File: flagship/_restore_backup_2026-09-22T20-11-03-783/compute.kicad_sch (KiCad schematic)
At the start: 1 part, among them U1 STAMP_P4

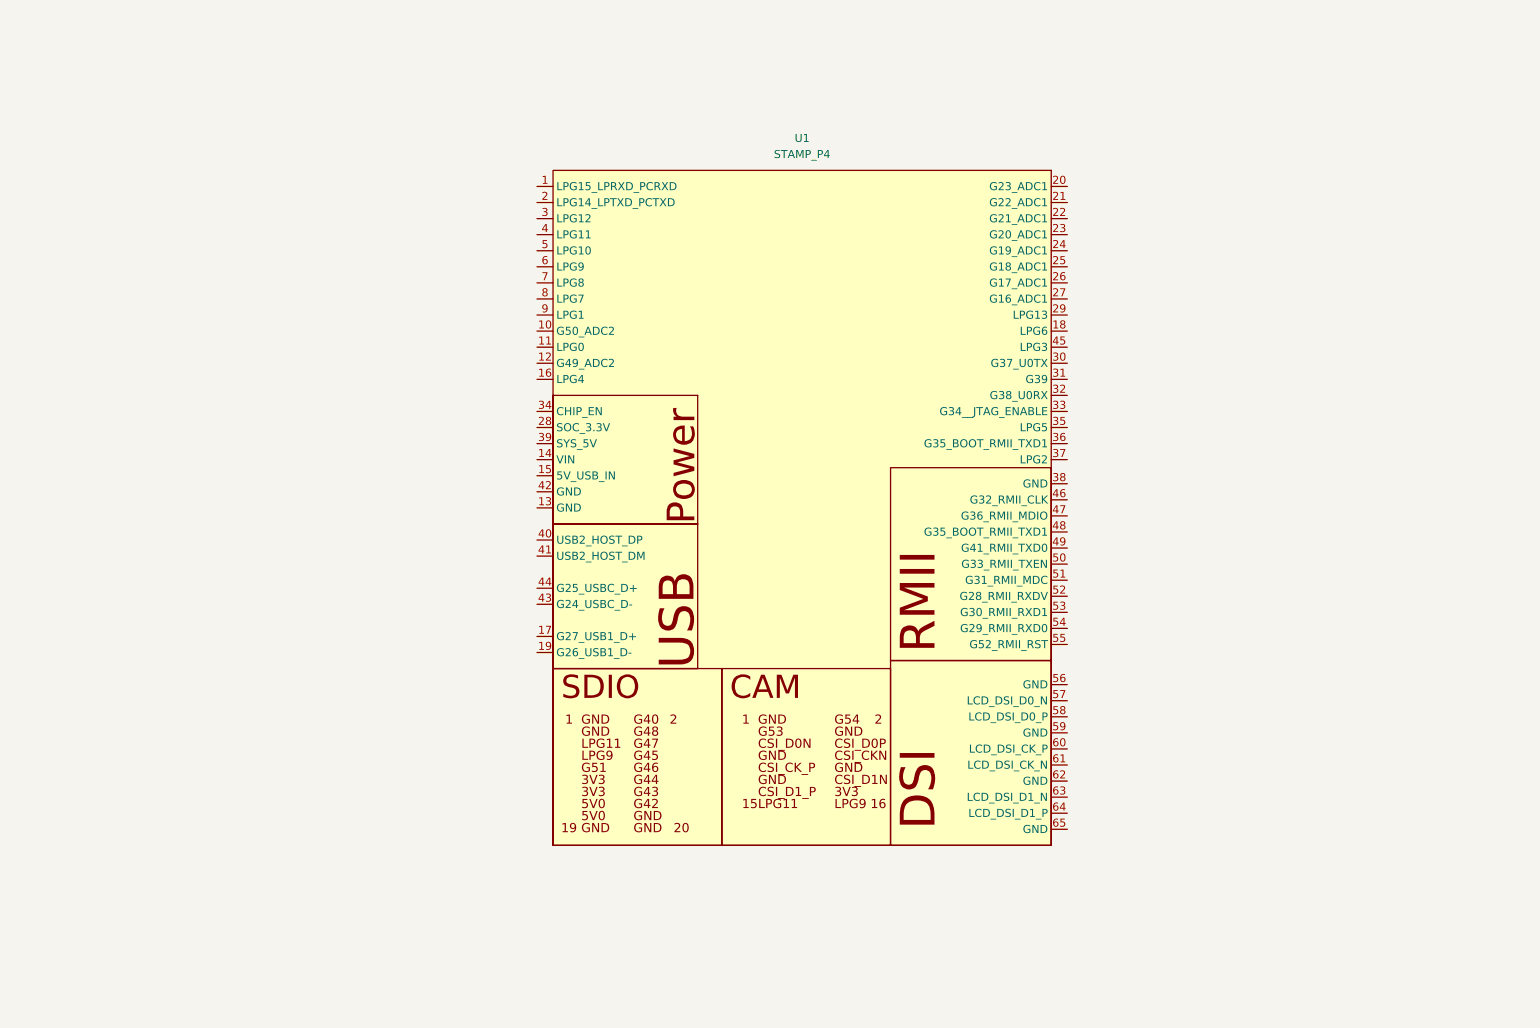
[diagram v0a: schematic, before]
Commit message: flagship: motor-switch note carries the measured 150 uF drive-side capacitance and the pre-charge numbers
Co-Authored-By: Claude Opus 5.5 (1M context) <noreply@anthropic.com>
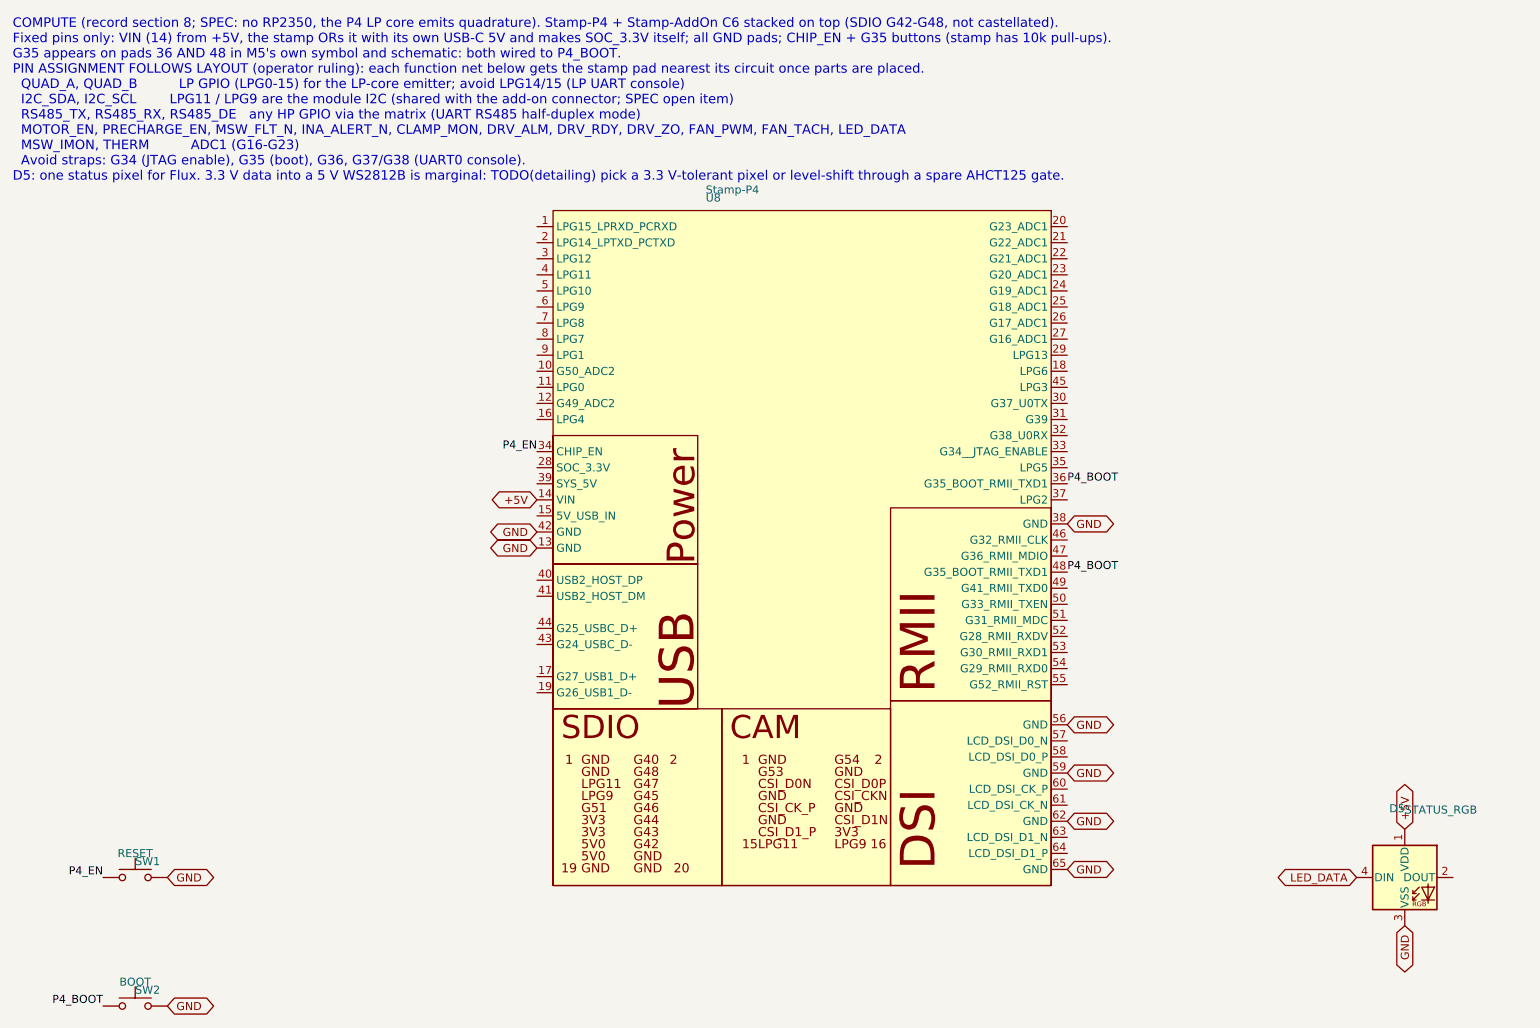
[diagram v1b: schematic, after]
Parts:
- removed U1: STAMP_P4, flagship:Stamp-P4, symbol m5stack:Stamp-P4
- added D5: STATUS_RGB, LED_SMD:LED_WS2812B_PLCC4_5.0x5.0mm_P3.2mm, symbol LED:WS2812B
- added SW1: RESET, symbol Switch:SW_Push
- added SW2: BOOT, symbol Switch:SW_Push
- added U8: Stamp-P4, flagship:Stamp-P4, symbol m5stack:Stamp-P4
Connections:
- new net +5V: D5.1 (VDD), U8.14 (VIN)
- new net GND: D5.3 (VSS), SW1.2, SW2.2, U8.13 (GND), U8.38 (GND), U8.42 (GND), U8.56 (GND), U8.59 (GND), U8.62 (GND), U8.65 (GND)
- new net LED_DATA: D5.4 (DIN)
- new net P4_BOOT: SW2.1, U8.36 (G35_BOOT_RMII_TXD1), U8.48 (G35_BOOT_RMII_TXD1)
- new net P4_EN: SW1.1, U8.34 (CHIP_EN)
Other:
- note added: "COMPUTE (record section 8; SPEC: no RP2350, the P4 LP core emits quadrature). Stamp-P4 + Stamp-AddOn C6 stacked on top (SDIO G42-G48, not castellated). Fixed pins only: VIN (14) from +5V, the stamp ORs it with its own USB-C 5V and makes SOC_3.3V itself; all GND pads; CHIP_EN + G35 buttons (stamp has 10k pull-ups). G35 appears on pads 36 AND 48 in M5's own symbol and schematic: both wired to P4_BO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"
